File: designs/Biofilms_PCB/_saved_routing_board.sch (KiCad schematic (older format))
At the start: 16 parts, among them J1 Arduino TL, J10 DC PWR, J11 Arduino IO, J12 Arduino Power Out, J2 Arduino BL, J3 Motor Power, J4 Arduino TR, J5 Arduino BR, J6 Servo, J7 Limit Switch, J8 Motor Driver, J9 Solenoid, Q1 Q_NPN_Darlington_BCE

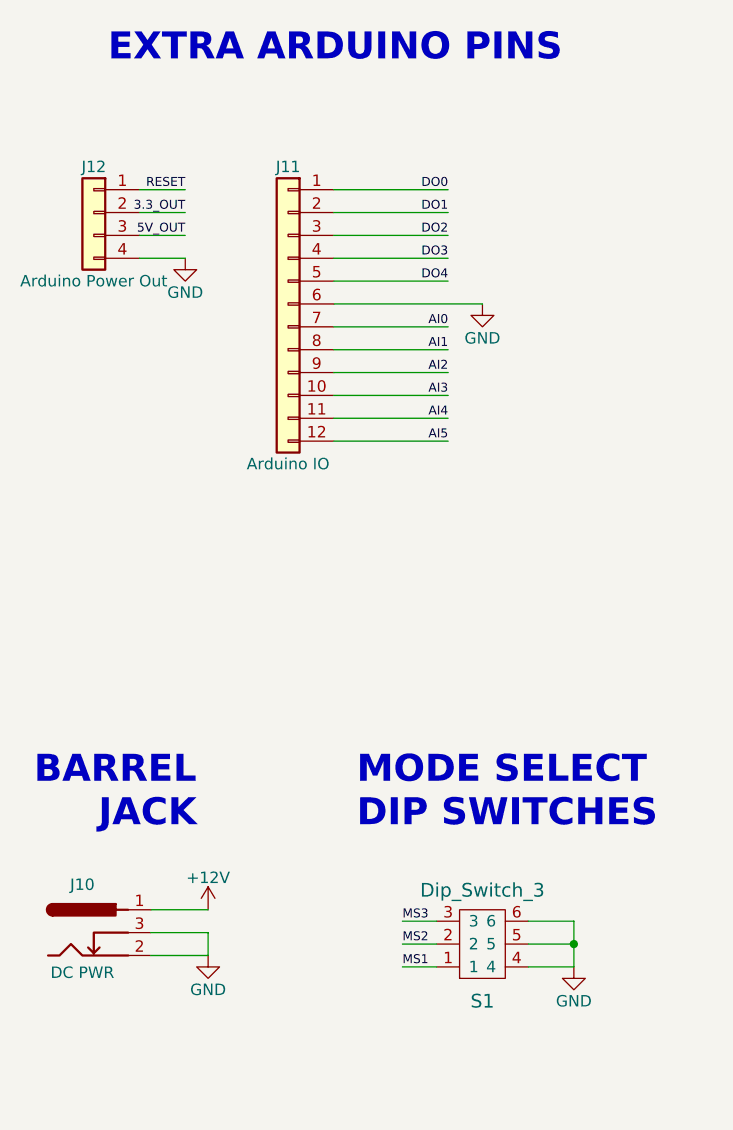
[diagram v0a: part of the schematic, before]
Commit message: finalized v1 of biofilms PCB
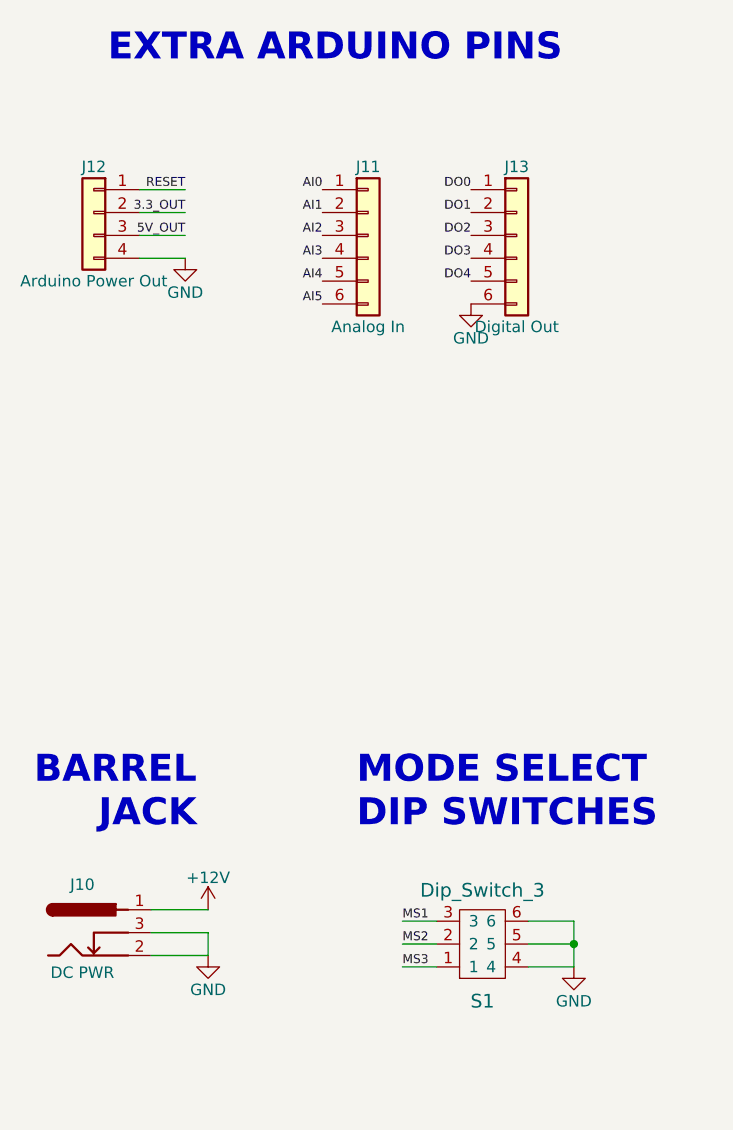
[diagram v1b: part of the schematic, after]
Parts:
- removed J11: Arduino IO, Socket_Strips:Socket_Strip_Straight_1x12_Pitch2.54mm, symbol Conn_01x12
- added J11: Analog In, Pin_Headers:Pin_Header_Straight_1x06_Pitch2.54mm, symbol Conn_01x06
- added J13: Digital Out, Pin_Headers:Pin_Header_Straight_1x06_Pitch2.54mm, symbol Conn_01x06
- D1: footprint (none) -> Diodes_SMD:D_SOD-123F
- J12: footprint (none) -> Pin_Headers:Pin_Header_Straight_1x04_Pitch2.54mm
- Q1: footprint (none) -> TO_SOT_Packages_SMD:SOT-23
- R1: footprint (none) -> Resistors_SMD:R_0603
- S1: footprint (none) -> Buttons_Switches_SMD:SW_DIP_x3_W8.61mm_Slide_LowProfile
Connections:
- net AI0: now also J11.1 (Pin_1)
- net AI1: now also J11.2 (Pin_2)
- net AI2: now also J11.3 (Pin_3)
- net AI3: now also J11.4 (Pin_4)
- net AI4: now also J11.5 (Pin_5)
- net AI5: now also J11.6 (Pin_6)
- net DO0: now also J13.1 (Pin_1)
- net DO1: now also J13.2 (Pin_2)
- net DO2: now also J13.3 (Pin_3)
- net DO3: now also J13.4 (Pin_4)
- net DO4: now also J13.5 (Pin_5)
- net GND: now also J13.6 (Pin_6)
- net MS1: now also S1.3; no longer S1.1
- net MS3: now also S1.1; no longer S1.3
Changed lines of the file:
@@
 NoConn ~ 1900 1900
-$Comp
-L Conn_01x12 J11
-U 1 1 5ADA8FB0
-P 8800 2450
-F 0 "J11" H 8800 3050 50  0000 C CNN
-F 1 "Arduino IO" H 8800 1750 50  0000 C CNN
-F 2 "Socket_Strips:Socket_Strip_Straight_1x12_Pitch2.54mm" H 8800 2450 50  0001 C CNN
-F 3 "" H 8800 2450 50  0001 C CNN
-	1    8800 2450
-	-1   0    0    -1
-$EndComp
 $Comp
 L GND #PWR01
@@
 L GND #PWR04
 U 1 1 5ADF80E8
-P 9650 2450
-F 0 "#PWR04" H 9650 2200 50  0001 C CNN
-F 1 "GND" H 9650 2300 50  0000 C CNN
-F 2 "" H 9650 2450 50  0001 C CNN
-F 3 "" H 9650 2450 50  0001 C CNN
-	1    9650 2450
+P 9600 2450
+F 0 "#PWR04" H 9600 2200 50  0001 C CNN
+F 1 "GND" H 9600 2300 50  0000 C CNN
+F 2 "" H 9600 2450 50  0001 C CNN
+F 3 "" H 9600 2450 50  0001 C CNN
+	1    9600 2450
 	1    0    0    -1
 $EndComp
@@
 Text Label 1600 2950 0    39   ~ 0
 AI0
-Text Label 9500 2050 2    39   ~ 0
+Text Label 9600 2050 2    39   ~ 0
 DO1
-Text Label 9500 1950 2    39   ~ 0
+Text Label 9600 1950 2    39   ~ 0
 DO0
-Text Label 9500 3050 2    39   ~ 0
+Text Label 8950 2450 2    39   ~ 0
 AI5
-Text Label 9500 2950 2    39   ~ 0
+Text Label 8950 2350 2    39   ~ 0
 AI4
-Text Label 9500 2850 2    39   ~ 0
+Text Label 8950 2250 2    39   ~ 0
 AI3
-Text Label 9500 2750 2    39   ~ 0
+Text Label 8950 2150 2    39   ~ 0
 AI2
-Text Label 9500 2650 2    39   ~ 0
+Text Label 8950 2050 2    39   ~ 0
 AI1
-Text Label 9500 2550 2    39   ~ 0
+Text Label 8950 1950 2    39   ~ 0
 AI0
 Text Label 2850 3050 0    39   ~ 0
@@
 	3300 2850 2850 2850
 Wire Wire Line
-	9500 3050 9000 3050
-Wire Wire Line
 	3300 2750 2850 2750
 Wire Wire Line
-	9500 2950 9000 2950
-Wire Wire Line
-	9000 2850 9500 2850
-Wire Wire Line
-	9500 2350 9000 2350
-Wire Wire Line
-	9500 2150 9000 2150
-Wire Wire Line
 	6450 2150 6100 2150
 Wire Wire Line
@@
 Wire Wire Line
 	1750 5250 2100 5250
-Wire Wire Line
-	9000 2250 9500 2250
 Wire Wire Line
 	3300 1950 2800 1950
@@
 Connection ~ 1500 2400
 Wire Wire Line
-	9000 1950 9500 1950
-Wire Wire Line
-	9000 2050 9500 2050
-Wire Wire Line
 	1900 2950 1600 2950
 Wire Wire Line
@@
 Wire Wire Line
 	1900 3450 1600 3450
-Wire Wire Line
-	9000 2450 9650 2450
-Wire Wire Line
-	9000 2550 9500 2550
-Wire Wire Line
-	9000 2650 9500 2650
-Wire Wire Line
-	9000 2750 9500 2750
 Wire Wire Line
 	2100 5350 1750 5350
@@
 F 0 "Q1" H 6630 5550 50  0000 L CNN
 F 1 "Q_NPN_Darlington_BCE" H 6630 5450 50  0000 L CNN
-F 2 "" H 6650 5600 50  0001 C CNN
+F 2 "TO_SOT_Packages_SMD:SOT-23" H 6650 5600 50  0001 C CNN
 F 3 "" H 6450 5500 50  0001 C CNN
 	1    6450 5500
@@
 F 0 "R1" V 6180 5500 50  0000 C CNN
 F 1 "10k" V 6100 5500 50  0000 C CNN
-F 2 "" V 6030 5500 50  0001 C CNN
+F 2 "Resistors_SMD:R_0603" V 6030 5500 50  0001 C CNN
 F 3 "" H 6100 5500 50  0001 C CNN
 	1    6100 5500
@@
 F 0 "D1" H 6550 5250 50  0000 C CNN
 F 1 "D" H 6550 5050 50  0000 C CNN
-F 2 "" H 6550 5150 50  0001 C CNN
+F 2 "Diodes_SMD:D_SOD-123F" H 6550 5150 50  0001 C CNN
 F 3 "" H 6550 5150 50  0001 C CNN
 	1    6550 5150
@@
 F 0 "S1" H 9650 5000 60  0000 C CNN
 F 1 "Dip_Switch_3" H 9650 5450 60  0000 C BNN
-F 2 "" V 9650 5250 60  0001 C CNN
+F 2 "Buttons_Switches_SMD:SW_DIP_x3_W8.61mm_Slide_LowProfile" V 9650 5250 60  0001 C CNN
 F 3 "" V 9650 5250 60  0001 C CNN
 	1    9650 5250
@@
 	9450 5350 9300 5350
 Text Label 9300 5350 0    39   ~ 0
-MS1
+MS3
 Text Label 9300 5250 0    39   ~ 0
 MS2
 Text Label 9300 5150 0    39   ~ 0
-MS3
+MS1
 Text Notes 9100 4750 0    118  ~ 24
 MODE SELECT\nDIP SWITCHES
-Text Label 9500 2150 2    39   ~ 0
+Text Label 9600 2150 2    39   ~ 0
 DO2
-Text Label 9500 2250 2    39   ~ 0
+Text Label 9600 2250 2    39   ~ 0
 DO3
-Text Label 9500 2350 2    39   ~ 0
+Text Label 9600 2350 2    39   ~ 0
 DO4
 $Comp
@@
 F 0 "J12" H 7950 2250 50  0000 C CNN
 F 1 "Arduino Power Out" H 7950 1750 50  0000 C CNN
-F 2 "" H 7950 2050 50  0001 C CNN
+F 2 "Pin_Headers:Pin_Header_Straight_1x04_Pitch2.54mm" H 7950 2050 50  0001 C CNN
 F 3 "" H 7950 2050 50  0001 C CNN
 	1    7950 2050
@@
 	1    0    0    -1
 $EndComp
+$Comp
+L Conn_01x06 J11
+U 1 1 5AE35C87
+P 9150 2150
+F 0 "J11" H 9150 2450 50  0000 C CNN
+F 1 "Analog In" H 9150 1750 50  0000 C CNN
+F 2 "Pin_Headers:Pin_Header_Straight_1x06_Pitch2.54mm" H 9150 2150 50  0001 C CNN
+F 3 "" H 9150 2150 50  0001 C CNN
+	1    9150 2150
+	1    0    0    -1
+$EndComp
+$Comp
+L Conn_01x06 J13
+U 1 1 5AE35E1C
+P 9800 2150
+F 0 "J13" H 9800 2450 50  0000 C CNN
+F 1 "Digital Out" H 9800 1750 50  0000 C CNN
+F 2 "Pin_Headers:Pin_Header_Straight_1x06_Pitch2.54mm" H 9800 2150 50  0001 C CNN
+F 3 "" H 9800 2150 50  0001 C CNN
+	1    9800 2150
+	1    0    0    -1
+$EndComp
